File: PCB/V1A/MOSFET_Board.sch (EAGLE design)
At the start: 276 parts, among them IC301 7805T, IC302 7805T, J301 TEMP, J302 +12V, J303 CTRL, J304 FAN_MOLEX4PIN, J305 FAN_MOLEX4PIN, J306 DUT+, J307 DUT-, Q201 SIRC10DP, Q202 SIRC10DP, Q203 BC817, Q204 BC817, Q205 SIRC10DP, Q206 SIRC10DP, Q207 BC817, Q208 BC807, Q209 BC817, Q210 BC807, Q211 IXTK102N65X2, Q212 IXTK102N65X2, Q301 BC817, Q302 BC817, Q401 BC807, Q402 BC807, Q403 BC807, Q404 BC807, Q405 BC807, Q406 BC807, Q407 BC807, Q408 BC807, Q409 BC807, Q410 BC807, Q411 BC807, Q412 BC807, Q413 BC807, Q414 BC807, U201 AD420, U202 AD420, U203 LT1014I, U204 LT1014I, U205 AD620, U206 AD620, U207 AD620, U208 AD620, U209 LTC1865L, U210 LTC1865L, U301 LP2985-3.1, U302 LP2985-3.1, U303 LP2985-3.1, U304 AD620, U305 LTC1865L, U306 LTC1865L, U307 MAX743, U401 HCPL-063N, U402 HCPL-063N, U403 HCPL-063N, U404 HCPL-063N, U405 HCPL-063N, U406 HCPL-063N, U407 HCPL-063N

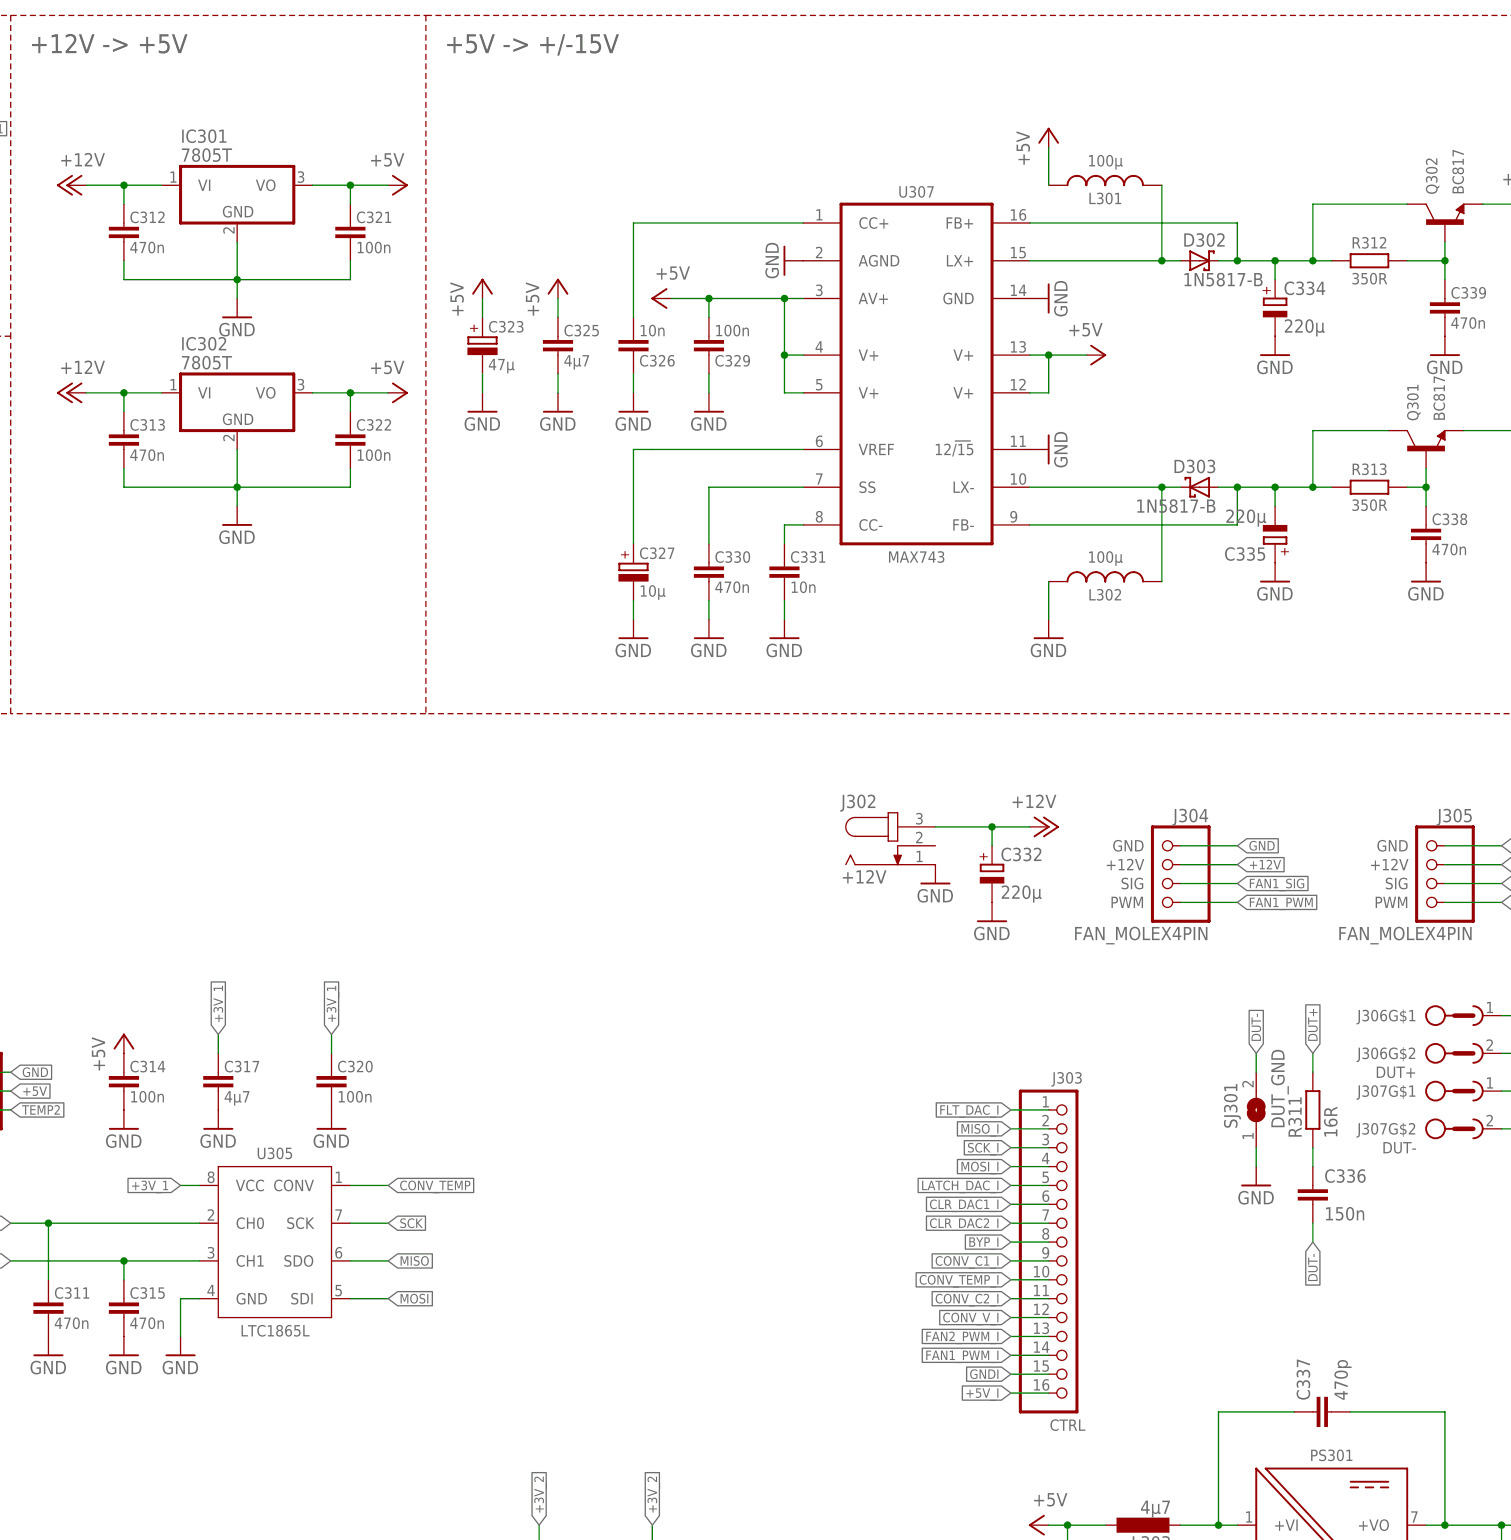
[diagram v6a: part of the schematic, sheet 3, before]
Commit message: PCB layout
Added some copper pours.
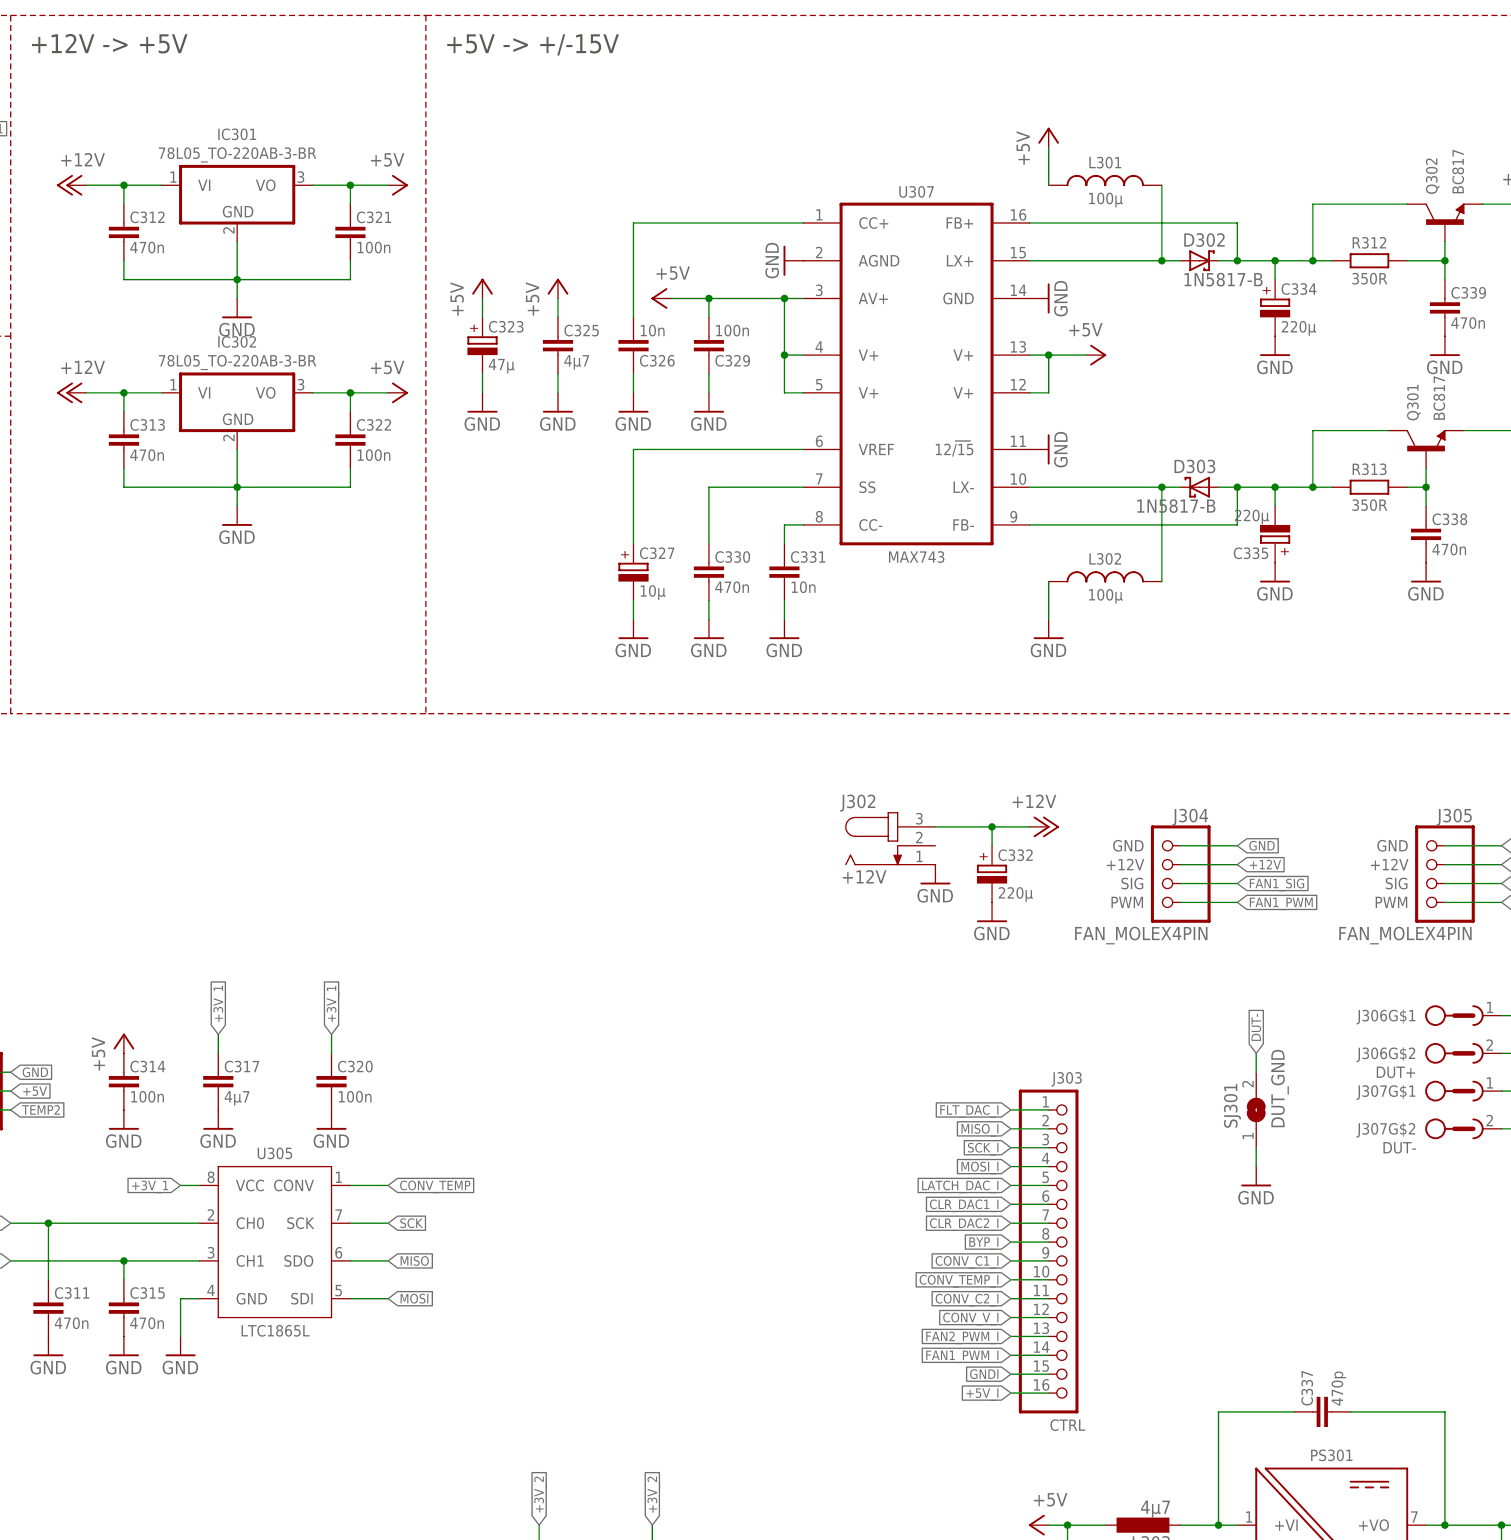
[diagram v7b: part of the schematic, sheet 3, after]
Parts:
- removed C336: 150n, rcl:C-EU050-030X075
- removed R311: 16R, rcl:R-EU_0204/7
- C332, C334, C335: device rcl:CPOL-EUE3.5-10 -> passives:CPOL_CAPPRD500W60D1000
- C337: device rcl:C-EU075-032X103 -> passives:C-EU_CAPRR1000W80L1300T400H900
- IC301, IC302: value 7805T -> 78L05_TO-220AB-3-BR; device linear:7805T -> ic:78L05_TO-220AB-3-BR
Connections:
- removed net N$61: C336.1, R311.1
- net DUT+: no longer R311.2
- net DUT-: no longer C336.2
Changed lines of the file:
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@@
 <part name="D303" library="diode" library_urn="urn:adsk.eagle:library:210" deviceset="1N581*" device="" package3d_urn="urn:adsk.eagle:package:43421/1" technology="7-B"/>
 <part name="L302" library="passives" deviceset="L-EU" device="_MSS1260" value="100µ"/>
-<part name="C334" library="rcl" library_urn="urn:adsk.eagle:library:334" deviceset="CPOL-EU" device="E3.5-10" package3d_urn="urn:adsk.eagle:package:23351/1" value="220µ"/>
+<part name="C334" library="passives" deviceset="CPOL" device="_CAPPRD500W60D1000" value="220µ"/>
 <part name="GND348" library="supply1" library_urn="urn:adsk.eagle:library:371" deviceset="GND" device=""/>
-<part name="C335" library="rcl" library_urn="urn:adsk.eagle:library:334" deviceset="CPOL-EU" device="E3.5-10" package3d_urn="urn:adsk.eagle:package:23351/1" value="220µ"/>
+<part name="C335" library="passives" deviceset="CPOL" device="_CAPPRD500W60D1000" value="220µ"/>
 <part name="P+317" library="supply1" library_urn="urn:adsk.eagle:library:371" deviceset="+15V" device=""/>
 <part name="P-303" library="supply1" library_urn="urn:adsk.eagle:library:371" deviceset="-15V" device=""/>
 <part name="J303" library="mechanical" deviceset="HEAD_1X16" device="_MALE" value="CTRL"/>
-<part name="IC301" library="linear" library_urn="urn:adsk.eagle:library:262" deviceset="78*" device="T" package3d_urn="urn:adsk.eagle:package:16414/1" technology="05"/>
+<part name="IC301" library="ic" deviceset="78L05" device="_TO-220AB-3-BR"/>
 <part name="P+308" library="supply1" library_urn="urn:adsk.eagle:library:371" deviceset="+5V" device=""/>
 <part name="P+304" library="supply1" library_urn="urn:adsk.eagle:library:371" deviceset="+12V" device=""/>
@@
 <part name="C321" library="passives" deviceset="C-EU" device="-1608" value="100n"/>
 <part name="GND322" library="supply1" library_urn="urn:adsk.eagle:library:371" deviceset="GND" device=""/>
-<part name="IC302" library="linear" library_urn="urn:adsk.eagle:library:262" deviceset="78*" device="T" package3d_urn="urn:adsk.eagle:package:16414/1" technology="05"/>
+<part name="IC302" library="ic" deviceset="78L05" device="_TO-220AB-3-BR"/>
 <part name="P+309" library="supply1" library_urn="urn:adsk.eagle:library:371" deviceset="+5V" device=""/>
 <part name="P+305" library="supply1" library_urn="urn:adsk.eagle:library:371" deviceset="+12V" device=""/>
@@
 <part name="GNDI418" library="supply1" library_urn="urn:adsk.eagle:library:371" deviceset="GNDI" device=""/>
 <part name="GND347" library="supply1" library_urn="urn:adsk.eagle:library:371" deviceset="GND" device=""/>
-<part name="R311" library="rcl" library_urn="urn:adsk.eagle:library:334" deviceset="R-EU_" device="0204/7" package3d_urn="urn:adsk.eagle:package:23498/1" value="16R"/>
-<part name="C336" library="rcl" library_urn="urn:adsk.eagle:library:334" deviceset="C-EU" device="050-030X075" package3d_urn="urn:adsk.eagle:package:23640/1" value="150n"/>
 <part name="D301" library="diode" library_urn="urn:adsk.eagle:library:210" deviceset="BAT54S" device="" package3d_urn="urn:adsk.eagle:package:43389/2"/>
 <part name="GND326" library="supply1" library_urn="urn:adsk.eagle:library:371" deviceset="GND" device=""/>
@@
 <part name="C304" library="passives" deviceset="C-EU" device="-1608" value="100n"/>
 <part name="GND307" library="supply1" library_urn="urn:adsk.eagle:library:371" deviceset="GND" device=""/>
-<part name="C337" library="rcl" library_urn="urn:adsk.eagle:library:334" deviceset="C-EU" device="075-032X103" package3d_urn="urn:adsk.eagle:package:23646/1" value="470p"/>
+<part name="C337" library="passives" deviceset="C-EU" device="_CAPRR1000W80L1300T400H900" value="470p"/>
 <part name="C340" library="passives" deviceset="C-EU" device="-1608" value="100n"/>
 <part name="C333" library="passives" deviceset="CPOL" device="-6032-C" value="10µ"/>
@@
 <part name="GND345" library="supply1" library_urn="urn:adsk.eagle:library:371" deviceset="GND" device=""/>
 <part name="GNDI302" library="supply1" library_urn="urn:adsk.eagle:library:371" deviceset="GNDI" device=""/>
-<part name="C332" library="rcl" library_urn="urn:adsk.eagle:library:334" deviceset="CPOL-EU" device="E3.5-10" package3d_urn="urn:adsk.eagle:package:23351/1" value="220µ"/>
+<part name="C332" library="passives" deviceset="CPOL" device="_CAPPRD500W60D1000" value="220µ"/>
 <part name="GND341" library="supply1" library_urn="urn:adsk.eagle:library:371" deviceset="GND" device=""/>
 <part name="SJ301" library="jumper" library_urn="urn:adsk.eagle:library:252" deviceset="SJ" device="W" package3d_urn="urn:adsk.eagle:package:15507/1" value="DUT_GND"/>
@@
 <instance part="P-303" gate="1" x="284.48" y="203.2" rot="MR270"/>
 <instance part="J303" gate="G$1" x="220.98" y="93.98"/>
-<instance part="IC301" gate="A1" x="109.22" y="236.22"/>
+<instance part="IC301" gate="G$1" x="109.22" y="236.22"/>
 <instance part="P+308" gate="1" x="132.08" y="236.22" rot="R270"/>
 <instance part="P+304" gate="1" x="86.36" y="236.22" rot="MR270"/>
@@
 <instance part="C321" gate="G$1" x="124.46" y="231.14"/>
 <instance part="GND322" gate="1" x="109.22" y="218.44"/>
-<instance part="IC302" gate="A1" x="109.22" y="208.28"/>
+<instance part="IC302" gate="G$1" x="109.22" y="208.28"/>
 <instance part="P+309" gate="1" x="132.08" y="208.28" rot="R270"/>
 <instance part="P+305" gate="1" x="86.36" y="208.28" rot="MR270"/>
@@
 <instance part="GND340" gate="1" x="203.2" y="142.24"/>
 <instance part="GND347" gate="1" x="246.38" y="101.6"/>
-<instance part="R311" gate="G$1" x="254" y="111.76" rot="R90"/>
-<instance part="C336" gate="G$1" x="254" y="101.6"/>
 <instance part="D301" gate="G$1" x="124.46" y="20.32"/>
 <instance part="GND326" gate="1" x="116.84" y="15.24"/>
@@
 <segment>
 <wire x1="93.98" y1="226.06" x2="93.98" y2="223.52" width="0.1524" layer="91"/>
-<pinref part="IC301" gate="A1" pin="GND"/>
+<pinref part="IC301" gate="G$1" pin="GND"/>
 <wire x1="109.22" y1="228.6" x2="109.22" y2="223.52" width="0.1524" layer="91"/>
 <wire x1="109.22" y1="223.52" x2="93.98" y2="223.52" width="0.1524" layer="91"/>
@@
 <segment>
 <wire x1="93.98" y1="198.12" x2="93.98" y2="195.58" width="0.1524" layer="91"/>
-<pinref part="IC302" gate="A1" pin="GND"/>
+<pinref part="IC302" gate="G$1" pin="GND"/>
 <wire x1="109.22" y1="200.66" x2="109.22" y2="195.58" width="0.1524" layer="91"/>
 <wire x1="109.22" y1="195.58" x2="93.98" y2="195.58" width="0.1524" layer="91"/>
@@
 </segment>
 <segment>
-<pinref part="IC301" gate="A1" pin="VO"/>
+<pinref part="IC301" gate="G$1" pin="VO"/>
 <wire x1="119.38" y1="236.22" x2="124.46" y2="236.22" width="0.1524" layer="91"/>
 <wire x1="124.46" y1="236.22" x2="124.46" y2="233.68" width="0.1524" layer="91"/>
@@
 </segment>
 <segment>
-<pinref part="IC302" gate="A1" pin="VO"/>
+<pinref part="IC302" gate="G$1" pin="VO"/>
 <wire x1="119.38" y1="208.28" x2="124.46" y2="208.28" width="0.1524" layer="91"/>
 <wire x1="124.46" y1="208.28" x2="124.46" y2="205.74" width="0.1524" layer="91"/>
@@
 <net name="+12V" class="0">
 <segment>
-<pinref part="IC301" gate="A1" pin="VI"/>
+<pinref part="IC301" gate="G$1" pin="VI"/>
 <wire x1="93.98" y1="236.22" x2="99.06" y2="236.22" width="0.1524" layer="91"/>
 <wire x1="93.98" y1="236.22" x2="93.98" y2="233.68" width="0.1524" layer="91"/>
@@
 </segment>
 <segment>
-<pinref part="IC302" gate="A1" pin="VI"/>
+<pinref part="IC302" gate="G$1" pin="VI"/>
 <wire x1="93.98" y1="208.28" x2="99.06" y2="208.28" width="0.1524" layer="91"/>
 <wire x1="93.98" y1="208.28" x2="93.98" y2="205.74" width="0.1524" layer="91"/>
@@
 <pinref part="J306" gate="G$2" pin="1"/>
 </segment>
-<segment>
-<pinref part="R311" gate="G$1" pin="2"/>
-<wire x1="254" y1="116.84" x2="254" y2="119.38" width="0.1524" layer="91"/>
-<label x="254" y="119.38" size="1.27" layer="95" font="vector" ratio="12" rot="R90" xref="yes"/>
-</segment>
 </net>
 <net name="DUT-" class="2">
@@
 <pinref part="SJ301" gate="1" pin="2"/>
 </segment>
-<segment>
-<pinref part="C336" gate="G$1" pin="2"/>
-<wire x1="254" y1="96.52" x2="254" y2="93.98" width="0.1524" layer="91"/>
-<label x="254" y="93.98" size="1.27" layer="95" font="vector" ratio="12" rot="R270" xref="yes"/>
-</segment>
 </net>
 <net name="FAN2_SIG" class="0">
@@
 </segment>
 </net>
-<net name="N$61" class="0">
-<segment>
-<pinref part="R311" gate="G$1" pin="1"/>
-<pinref part="C336" gate="G$1" pin="1"/>
-<wire x1="254" y1="106.68" x2="254" y2="104.14" width="0.1524" layer="91"/>
-</segment>
-</net>
 <net name="VREF_MAX743" class="0">
 <segment>
@@
 packages will not be understood (or retained) with this version.
 </note>
-<note version="8.4" severity="warning">
-Since Version 8.4, EAGLE supports properties for SPICE simulation.
-Probes in schematics and SPICE mapping objects found in parts and library devices
-will not be understood with this version. Update EAGLE to the latest version
-for full support of SPICE simulation.
-</note>
 </compatibility>

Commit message: PCB layout
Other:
- moved on the sheet: C201, C202, C203, C204, C205, C206, C207, C208, C209, C210, C211, C212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
